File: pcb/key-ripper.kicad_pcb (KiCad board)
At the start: 2 copper layers, 285.8 x 116.7 mm, 193 parts, among them J1 Conn_01x04, SW1 ESC, SW10 F9, SW11 F10, SW12 F11, SW13 F12, SW14 TILDE, SW15 1, SW16 2, SW17 3, SW18 4, SW19 5, SW2 F1, SW20 6, SW21 7, SW22 8, SW23 9, SW24 0, SW25 -, SW26 +, SW27 BACKSPACE, SW28 TAB, SW29 Q, SW3 F2, SW30 W, SW31 E, SW32 R, SW33 T, SW34 Y, SW35 U, SW36 I, SW37 O, SW38 P, SW39 [, SW4 F3, SW40 ], SW41 BACKSLASH, SW42 CAPS, SW43 A, SW44 S, SW45 D, SW46 F, SW47 G, SW48 H, SW49 J, SW5 F4, SW50 K, SW51 L, SW52 ;, SW53 ', SW54 ENTER, SW55 L_SHIFT, SW56 Z, SW57 X, SW58 C, SW59 V, SW6 F5, SW60 B, SW61 N, SW62 M, SW63 ,, SW64 ., SW65 FWD_SLASH, SW66 UP, SW67 FN, SW68 BL_CTRL, SW69 L_ALT, SW7 F6, SW70 L_CMD, SW71 SPACE, SW72 R_CMD, SW73 LEFT, SW74 DOWN, SW75 RIGHT, SW8 F7, SW9 F8, U1 RP2040, U2 TYPE-C-31-M-12, U3 XC6206PxxxMR, U4 W25Q128JVS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

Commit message: Everything is ready to be routed
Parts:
- moved U6 48.9 mm to (143.3, 80.8)
- moved C18 48.5 mm to (138.0, 82.1)
- moved U5 41.9 mm to (82.9, 74.4), turned to 180 degrees
- moved J1 38.2 mm to (116.6, 68.9)
- moved R8 37.4 mm to (136.7, 82.1)
- moved R5 30.8 mm to (88.0, 75.7), turned to -90 degrees
- moved C6 0.54 mm to (112.5, 71.2)
- moved C7 0.54 mm to (115.3, 73.4)
- moved R3 0.54 mm to (112.7, 75.7)
- moved Y1 0.54 mm to (112.6, 73.4)
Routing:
- net RUN: track 0.00 -> 34.6 mm
- net SWCLK: track 0.00 -> 14.2 mm, vias 0 -> 1
- net SWD: track 0.00 -> 13.4 mm, vias 0 -> 1
- net QSPI_SS: track 5.71 -> 19.0 mm
- net OSC_OUT: track 0.00 -> 7.45 mm
- net XOUT_MCU: track 0.00 -> 4.76 mm
- net OSC_IN: track 0.00 -> 4.25 mm

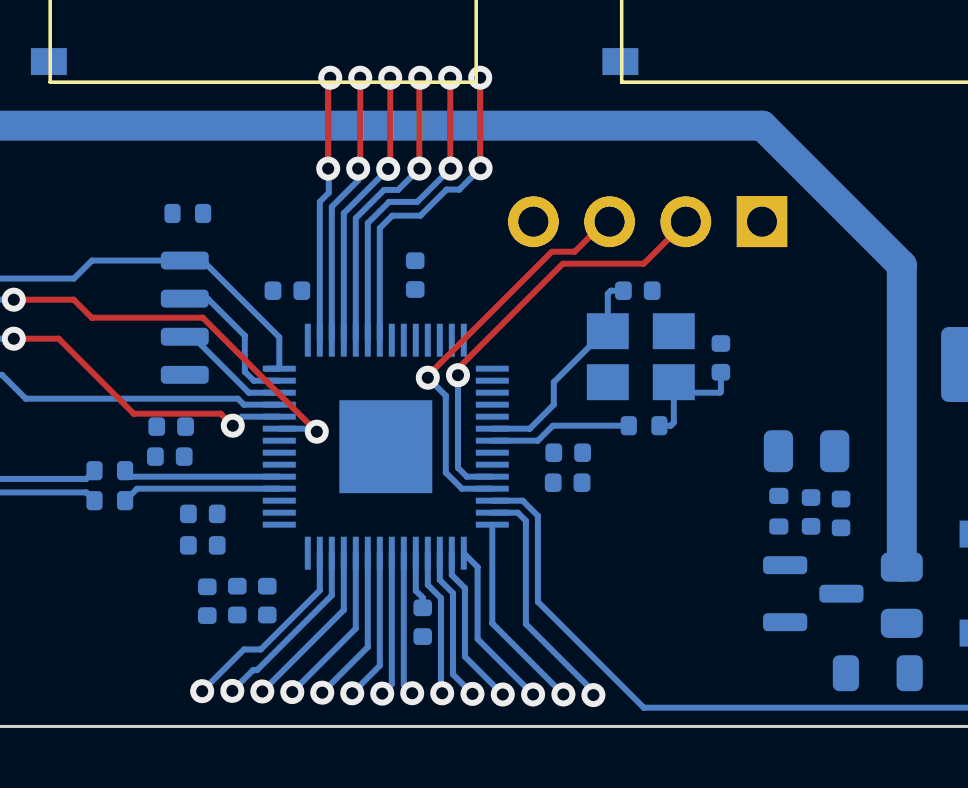
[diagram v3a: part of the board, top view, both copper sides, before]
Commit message: Start routing power, simplify SWD connector
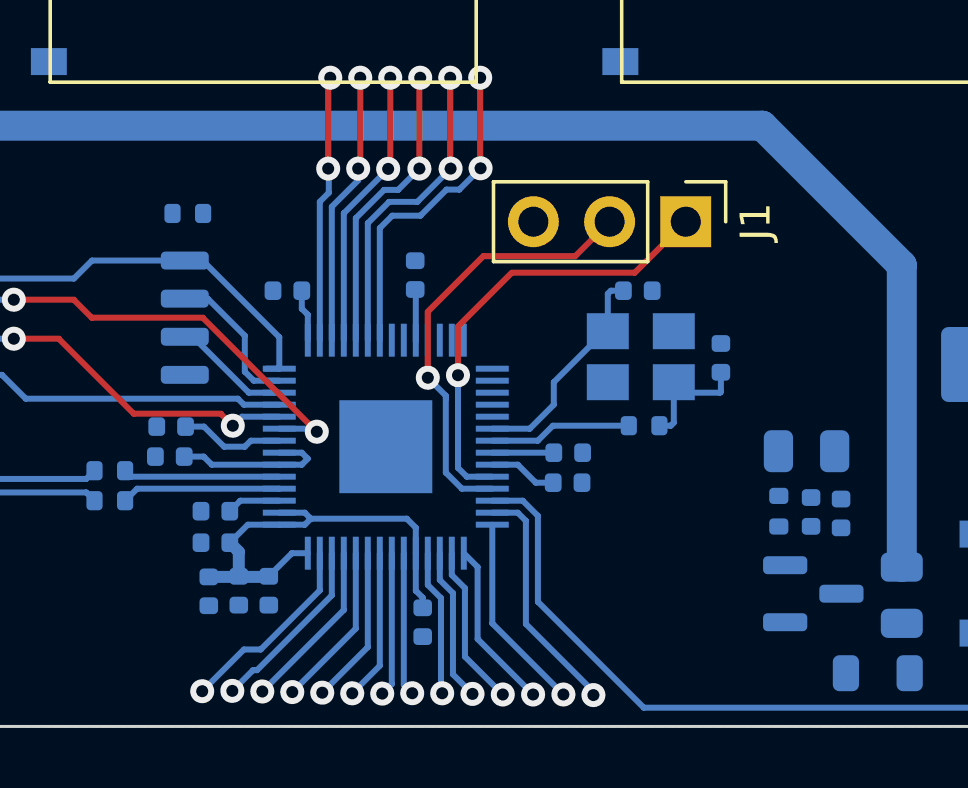
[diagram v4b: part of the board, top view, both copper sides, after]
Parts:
- J1: value Conn_01x04 -> Conn_01x03; footprint Connector_PinHeader_2.54mm:PinHeader_1x04_P2.54mm_Vertical -> Connector_PinHeader_2.54mm:PinHeader_1x03_P2.54mm_Vertical; moved to F.Cu
- moved J1 2.54 mm to (114.1, 68.9), turned to -90 degrees
- moved C2 0.43 mm to (98.4, 78.5)
- moved C8 0.43 mm to (98.4, 79.6)
- moved C1 0.33 mm to (98.2, 81.2)
- moved C15 0.33 mm to (100.2, 81.2)
- moved C9 0.33 mm to (99.2, 81.2)
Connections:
- J1 pad 1: +3V3 -> SWCLK
- J1 pad 2: SWCLK -> SWD
- J1 pad 3: SWD -> GND
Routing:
- net +3V3: track 1.92 -> 26.3 mm
- net +1V1: track 0.00 -> 7.56 mm
- net SWD: track 13.4 -> 14.7 mm
- net SWCLK: track 14.2 -> 15.0 mm

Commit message: More power routing
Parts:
- moved R8 20.9 mm to (115.8, 83.3)
- moved J1 9.42 mm to (113.5, 78.3), turned to 0 degrees
- moved C17 1.11 mm to (111.2, 78.0)
- moved U5 0.80 mm to (82.9, 73.6)
- moved R5 0.80 mm to (88.0, 74.9)
- moved C11 0.56 mm to (110.7, 76.4)
- moved C16 0.43 mm to (96.9, 75.3)
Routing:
- net +3V3: track 26.3 -> 127.5 mm
- net +1V1: track 7.56 -> 23.4 mm, vias 0 -> 2
- net SWD: track 14.7 -> 7.89 mm, vias 1 -> 0
- net SWCLK: track 15.0 -> 8.22 mm, vias 1 -> 0
- net RUN: track 34.6 -> 39.8 mm
- net Net-(D76-Pad1): track 184.6 -> 181.5 mm
- net QSPI_SS: track 19.0 -> 18.2 mm
- net ROW4: track 10.4 -> 11.1 mm
- net ROW2: track 9.39 -> 10.1 mm
- net ROW1: track 9.14 -> 9.84 mm
- net ROW3: track 9.91 -> 10.6 mm
- net ROW0: track 8.91 -> 9.59 mm

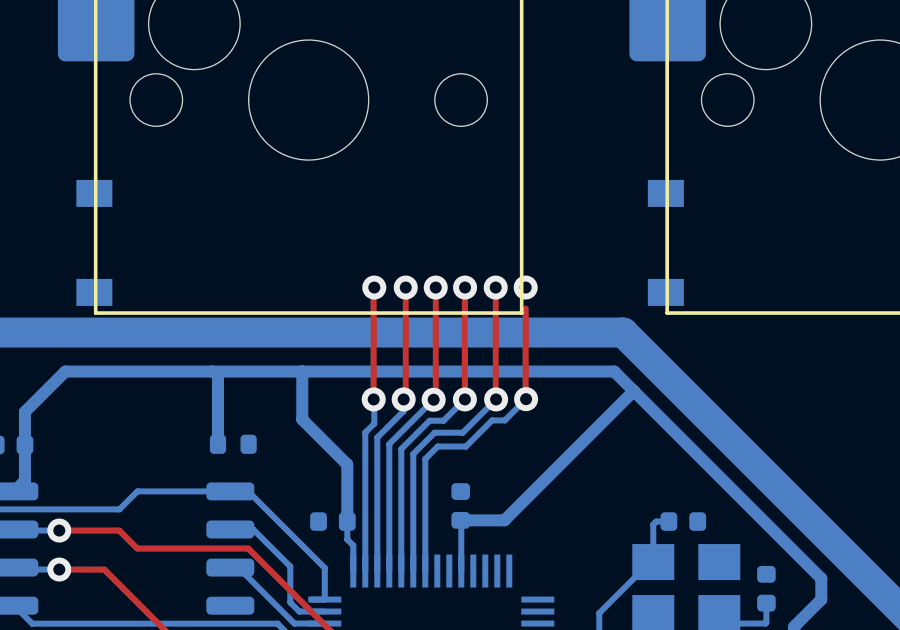
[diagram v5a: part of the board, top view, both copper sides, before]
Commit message: Move row vias up a bit
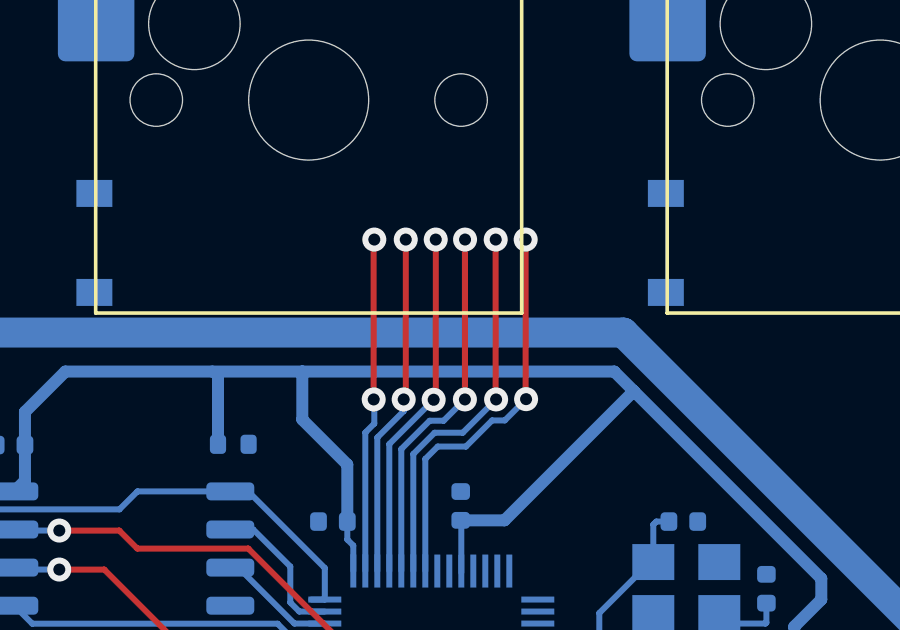
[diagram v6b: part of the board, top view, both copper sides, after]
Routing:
- net ROW5: track 10.9 -> 13.2 mm
- net ROW4: track 11.1 -> 12.7 mm
- net ROW3: track 10.6 -> 12.2 mm
- net ROW2: track 10.1 -> 11.7 mm
- net ROW0: track 9.59 -> 11.2 mm
- net ROW1: track 9.84 -> 11.4 mm
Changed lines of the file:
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@@
   (segment (start 115.9 85.1) (end 125 85.1) (width 0.2) (layer "B.Cu") (net 6))
   (segment (start 108.663965 78.199848) (end 107.650038 78.199848) (width 0.2) (layer "B.Cu") (net 6))
-  (segment (start 102.18 67.13) (end 102.18 63.42) (width 0.2) (layer "F.Cu") (net 7))
-  (segment (start 102.18 63.42) (end 102.2 63.4) (width 0.2) (layer "F.Cu") (net 7))
+  (segment (start 102.18 67.13) (end 102.18 61.82) (width 0.2) (layer "F.Cu") (net 7))
+  (segment (start 102.18 61.82) (end 102.2 61.8) (width 0.2) (layer "F.Cu") (net 7))
   (via (at 102.18 67.13) (size 0.8) (drill 0.4) (layers "F.Cu" "B.Cu") (net 7))
-  (via (at 102.2 63.4) (size 0.8) (drill 0.4) (layers "F.Cu" "B.Cu") (net 7))
+  (via (at 102.2 61.8) (size 0.8) (drill 0.4) (layers "F.Cu" "B.Cu") (net 7))
   (segment (start 101.899975 68.235019) (end 102.2 67.934994) (width 0.2) (layer "B.Cu") (net 7))
   (segment (start 102.2 67.934994) (end 102.2 67.15) (width 0.2) (layer "B.Cu") (net 7))
   (segment (start 101.899975 72.849835) (end 101.899975 68.235019) (width 0.2) (layer "B.Cu") (net 7))
   (segment (start 102.2 67.15) (end 102.18 67.13) (width 0.2) (layer "B.Cu") (net 7))
-  (segment (start 103.248327 67.061176) (end 103.248327 63.4) (width 0.2) (layer "F.Cu") (net 21))
+  (segment (start 103.248327 67.061176) (end 103.248327 61.8) (width 0.2) (layer "F.Cu") (net 21))
   (segment (start 103.179503 67.13) (end 103.248327 67.061176) (width 0.2) (layer "F.Cu") (net 21))
-  (via (at 103.248327 63.4) (size 0.8) (drill 0.4) (layers "F.Cu" "B.Cu") (net 21))
+  (via (at 103.248327 61.8) (size 0.8) (drill 0.4) (layers "F.Cu" "B.Cu") (net 21))
   (via (at 103.179503 67.13) (size 0.8) (drill 0.4) (layers "F.Cu" "B.Cu") (net 21))
   (segment (start 102.300025 68.399975) (end 103.179503 67.520497) (width 0.2) (layer "B.Cu") (net 21))
@@
   (segment (start 103.179503 67.520497) (end 103.179503 67.13) (width 0.2) (layer "B.Cu") (net 21))
   (segment (start 104.178955 67.140051) (end 104.24783 67.071176) (width 0.2) (layer "F.Cu") (net 37))
-  (segment (start 104.24783 67.071176) (end 104.24783 63.4) (width 0.2) (layer "F.Cu") (net 37))
-  (via (at 104.24783 63.4) (size 0.8) (drill 0.4) (layers "F.Cu" "B.Cu") (net 37))
+  (segment (start 104.24783 67.071176) (end 104.24783 61.8) (width 0.2) (layer "F.Cu") (net 37))
+  (via (at 104.24783 61.8) (size 0.8) (drill 0.4) (layers "F.Cu" "B.Cu") (net 37))
   (via (at 104.178955 67.140051) (size 0.8) (drill 0.4) (layers "F.Cu" "B.Cu") (net 37))
   (segment (start 102.700076 68.61893) (end 104.178955 67.140051) (width 0.2) (layer "B.Cu") (net 37))
   (segment (start 102.700076 72.849835) (end 102.700076 68.61893) (width 0.2) (layer "B.Cu") (net 37))
-  (segment (start 105.22 67.13) (end 105.22 63.405) (width 0.2) (layer "F.Cu") (net 53))
-  (segment (start 105.22 63.405) (end 105.225 63.4) (width 0.2) (layer "F.Cu") (net 53))
-  (via (at 105.225 63.4) (size 0.8) (drill 0.4) (layers "F.Cu" "B.Cu") (net 53))
+  (segment (start 105.22 67.13) (end 105.22 61.805) (width 0.2) (layer "F.Cu") (net 53))
+  (segment (start 105.22 61.805) (end 105.225 61.8) (width 0.2) (layer "F.Cu") (net 53))
+  (via (at 105.225 61.8) (size 0.8) (drill 0.4) (layers "F.Cu" "B.Cu") (net 53))
   (via (at 105.22 67.13) (size 0.8) (drill 0.4) (layers "F.Cu" "B.Cu") (net 53))
   (segment (start 104.510448 67.839552) (end 105.22 67.13) (width 0.2) (layer "B.Cu") (net 53))
@@
   (segment (start 104.044448 67.839552) (end 104.510448 67.839552) (width 0.2) (layer "B.Cu") (net 53))
   (segment (start 103.099873 72.849835) (end 103.099873 68.784127) (width 0.2) (layer "B.Cu") (net 53))
-  (segment (start 106.246836 67.116836) (end 106.246836 63.4) (width 0.2) (layer "F.Cu") (net 67))
+  (segment (start 106.246836 67.116836) (end 106.246836 61.8) (width 0.2) (layer "F.Cu") (net 67))
   (segment (start 106.26 67.13) (end 106.246836 67.116836) (width 0.2) (layer "F.Cu") (net 67))
-  (via (at 106.246836 63.4) (size 0.8) (drill 0.4) (layers "F.Cu" "B.Cu") (net 67))
+  (via (at 106.246836 61.8) (size 0.8) (drill 0.4) (layers "F.Cu" "B.Cu") (net 67))
   (via (at 106.26 67.13) (size 0.8) (drill 0.4) (layers "F.Cu" "B.Cu") (net 67))
   (segment (start 104.209931 68.239063) (end 105.150937 68.239063) (width 0.2) (layer "B.Cu") (net 67))
@@
   (segment (start 103.499924 68.94907) (end 104.209931 68.239063) (width 0.2) (layer "B.Cu") (net 67))
   (segment (start 105.150937 68.239063) (end 106.26 67.13) (width 0.2) (layer "B.Cu") (net 67))
-  (segment (start 107.246339 67.106792) (end 107.246339 64.1005) (width 0.2) (layer "F.Cu") (net 81))
+  (segment (start 107.246339 67.106792) (end 107.246339 61.8) (width 0.2) (layer "F.Cu") (net 81))
   (segment (start 107.259452 67.119905) (end 107.246339 67.106792) (width 0.2) (layer "F.Cu") (net 81))
   (via (at 107.259452 67.119905) (size 0.8) (drill 0.4) (layers "F.Cu" "B.Cu") (net 81))
-  (via (at 107.246339 63.4) (size 0.8) (drill 0.4) (layers "F.Cu" "B.Cu") (net 81))
+  (via (at 107.246339 61.8) (size 0.8) (drill 0.4) (layers "F.Cu" "B.Cu") (net 81))
   (segment (start 106.125495 67.829511) (end 106.549846 67.829511) (width 0.2) (layer "B.Cu") (net 81))
   (segment (start 105.255006 68.7) (end 106.125495 67.829511) (width 0.2) (layer "B.Cu") (net 81))

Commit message: Move the diodes to a better spot
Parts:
- moved D1 11.3 mm to (-7.50, -25.6), turned to -90 degrees
- moved D10 11.3 mm to (202.1, -25.6), turned to -90 degrees
- moved D11 11.3 mm to (221.1, -25.6), turned to -90 degrees
- moved D12 11.3 mm to (240.2, -25.6), turned to -90 degrees
- moved D13 11.3 mm to (259.2, -25.6), turned to -90 degrees
- moved D2 11.3 mm to (28.2, -25.6), turned to -90 degrees
- moved D3 11.3 mm to (47.3, -25.6), turned to -90 degrees
- moved D4 11.3 mm to (66.3, -25.6), turned to -90 degrees
- moved D5 11.3 mm to (85.4, -25.6), turned to -90 degrees
- moved D6 11.3 mm to (113.9, -25.6), turned to -90 degrees
- moved D7 11.3 mm to (135.4, -25.6), turned to -90 degrees
- moved D8 11.3 mm to (154.4, -25.6), turned to -90 degrees
- moved D9 11.3 mm to (173.5, -25.6), turned to -90 degrees
- moved D14 11.3 mm to (-7.50, -6.55), turned to -90 degrees
- moved D15 11.3 mm to (11.6, -6.55), turned to -90 degrees
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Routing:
- net Net-(D76-Pad1): track 181.5 -> 0.00 mm
- net USB-: track 182.7 -> 22.6 mm
- net USB+: track 180.7 -> 21.5 mm

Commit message: Start moving the chip around again...
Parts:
- moved F1 137.6 mm to (24.7, -16.6)
- moved C10 99.8 mm to (12.9, 44.4), turned to 180 degrees
- moved C17 97.6 mm to (17.8, 49.7), turned to -90 degrees
- moved C11 95.7 mm to (18.8, 49.7), turned to -90 degrees
- moved C15 95.7 mm to (14.2, 39.3), turned to 180 degrees
- moved FB1 95.6 mm to (33.1, 45.1), turned to -90 degrees
- moved R3 95.5 mm to (19.6, 54.3), turned to 90 degrees
- moved C9 95.2 mm to (14.2, 38.3), turned to 180 degrees
- moved C4 94.9 mm to (31.1, 43.4)
- moved C5 94.9 mm to (30.1, 43.4)
- moved D77 94.9 mm to (30.0, 41.4)
- moved R9 94.9 mm to (29.1, 43.4)
- moved U3 94.9 mm to (30.2, 46.1)
- moved C7 94.9 mm to (21.9, 56.9), turned to 0 degrees
- moved C1 94.8 mm to (14.2, 37.3), turned to 180 degrees
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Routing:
- net Net-(F1-Pad2): track 0.00 -> 72.8 mm
- net USB-: track 22.6 -> 70.4 mm
- net USB+: track 21.5 -> 69.1 mm
- net QSPI_SD3: track 14.4 -> 36.1 mm
- net QSPI_SCLK: track 11.7 -> 30.7 mm
- net QSPI_SD0: track 10.8 -> 25.6 mm
- net QSPI_SS: track 18.2 -> 26.6 mm
- net QSPI_SD1: track 4.99 -> 12.9 mm
- net OSC_OUT: track 7.45 -> 15.2 mm
- net QSPI_SD2: track 3.92 -> 11.4 mm
- net XOUT_MCU: track 4.76 -> 11.9 mm
- net USB_MCU-: track 5.31 -> 10.6 mm
- net USB_MCU+: track 5.22 -> 10.5 mm
